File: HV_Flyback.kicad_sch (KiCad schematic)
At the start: 21 parts, among them J3 Conn_Coaxial, J4 Conn_01x01_Female, J5 Conn_01x01_Female, Q1 AON7296, U2 LT3750A, U4 AD5170BRMZ2.5

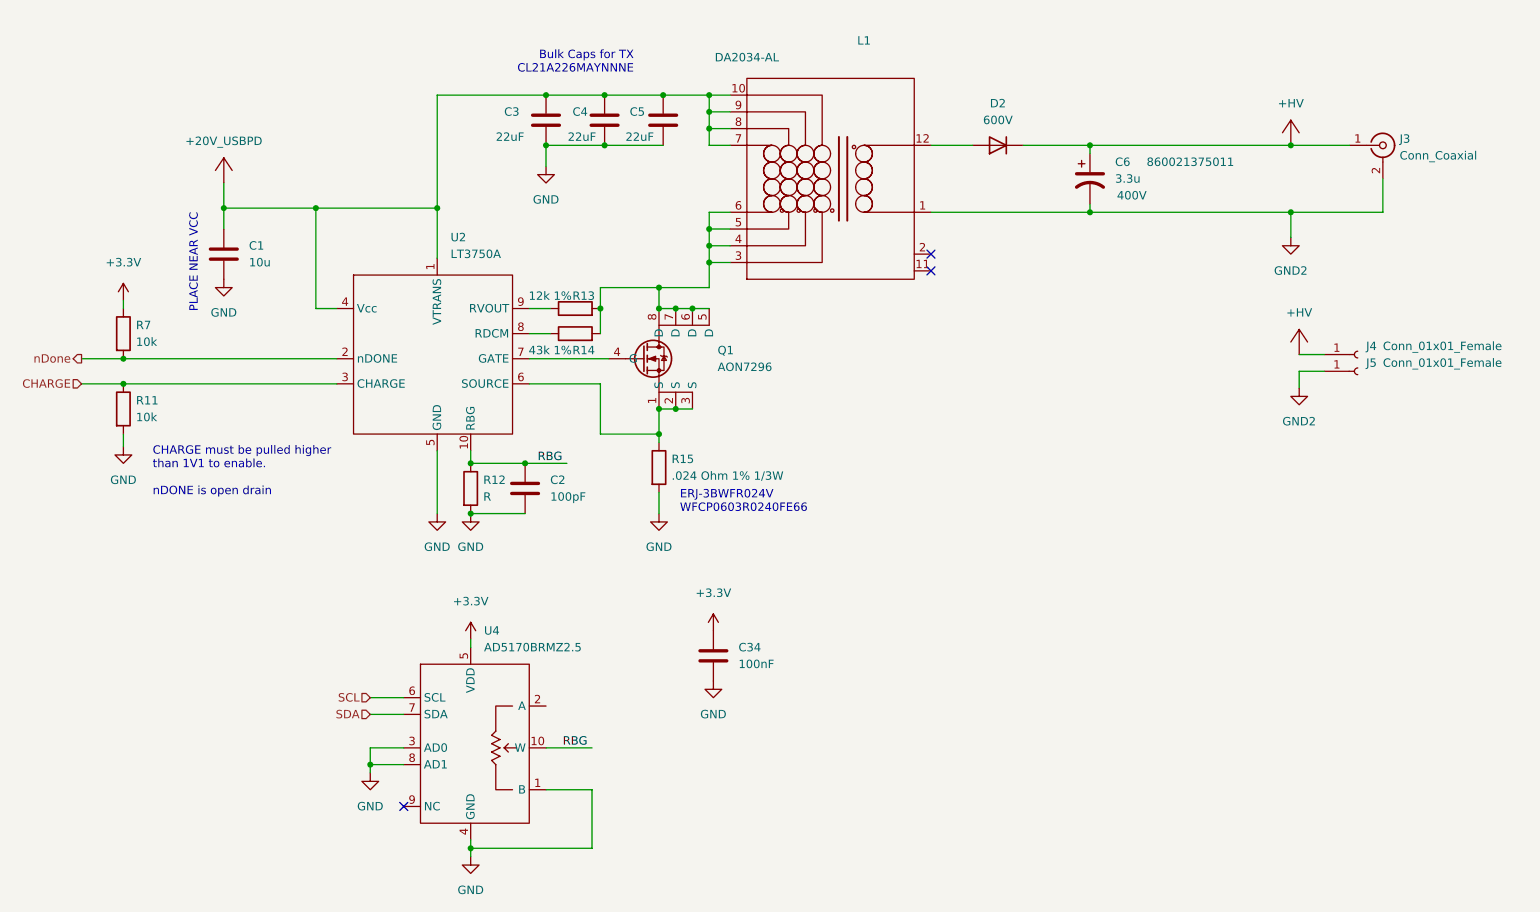
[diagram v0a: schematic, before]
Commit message: finished routing, sending to fab
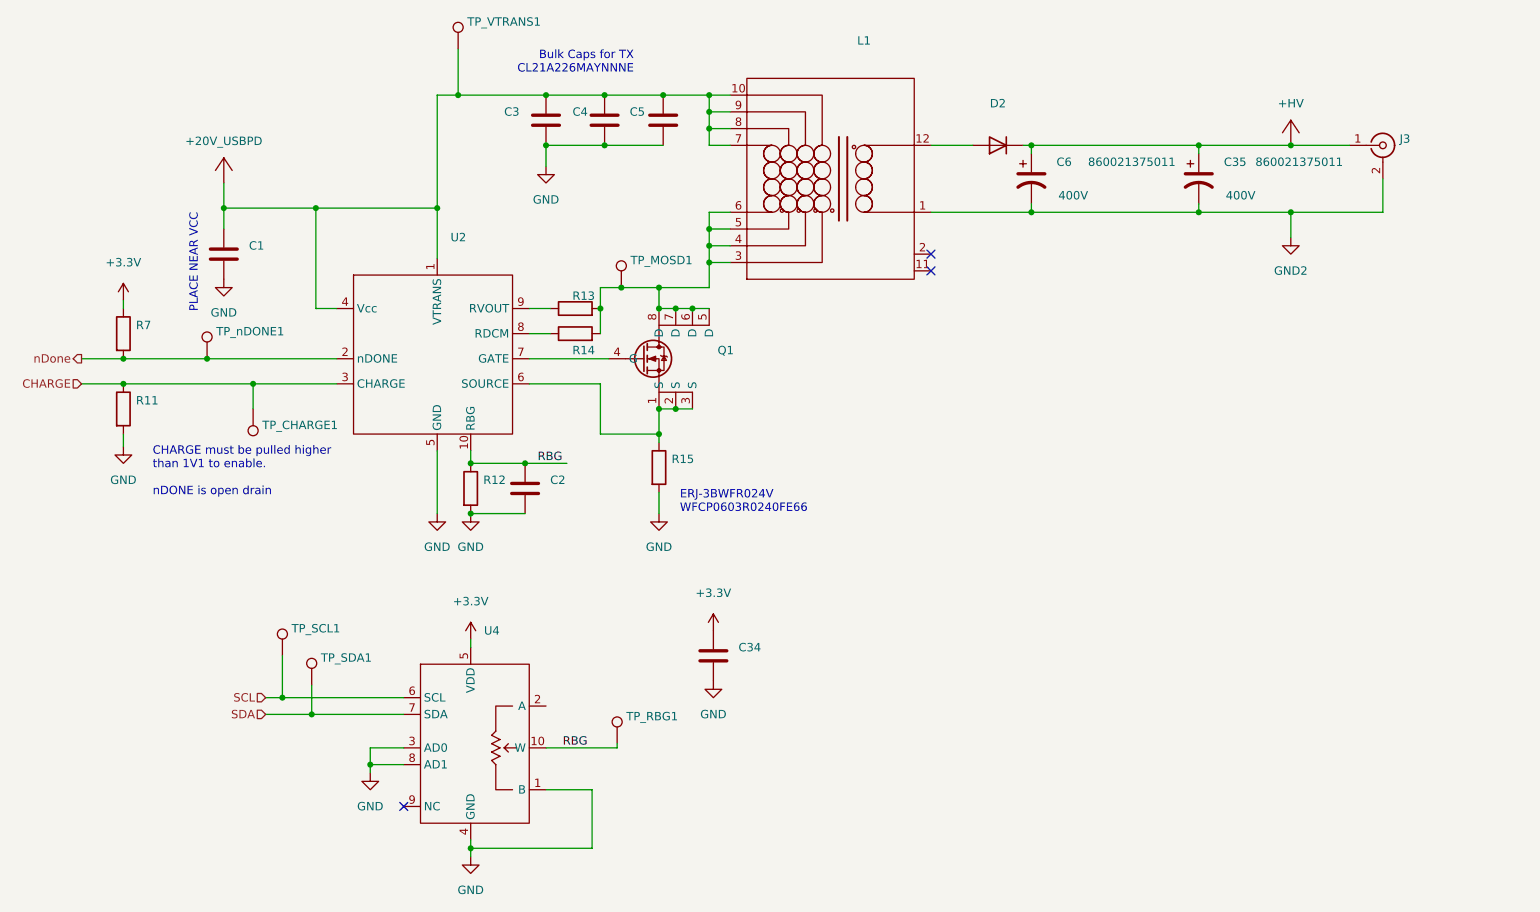
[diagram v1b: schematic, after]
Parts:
- removed J4: Conn_01x01_Female, PD_HV_footprints:CalTest_CT3151-2, symbol Connector:Conn_01x01_Female
- removed J5: Conn_01x01_Female, PD_HV_footprints:CalTest_CT3151-0, symbol Connector:Conn_01x01_Female
- added C35: (no value), symbol Device:C_Polarized_US
- added TP_CHARGE1, TP_MOSD1, TP_RBG1, TP_SCL1, TP_SDA1, TP_VTRANS1, TP_nDONE1: (no value), symbol Connector:TestPoint
- C1: value 10u -> (none); footprint Capacitor_SMD:C_0603_1608Metric -> (none)
- C2: value 100pF -> (none); footprint Capacitor_SMD:C_0603_1608Metric -> (none)
- C3, C4, C5: value 22uF -> (none); footprint Capacitor_SMD:C_0805_2012Metric -> (none)
- C34: value 100nF -> (none); footprint Capacitor_SMD:C_0603_1608Metric -> (none)
- C6: value 3.3u -> (none); footprint Capacitor_THT:CP_Radial_D10.0mm_P5.00mm -> (none)
- D2: value 600V -> (none); footprint Diode_SMD:D_SMA -> (none)
- J3: value Conn_Coaxial -> (none); footprint PD_HV_footprints:TE_5227161-2 -> (none)
- L1: value DA2034-AL -> (none); footprint PD_HV_footprints:DA2034-AL -> (none)
- Q1: value AON7296 -> (none); footprint PD_HV_footprints:DFN3X3A_8L_EPA1_P_AOS -> (none)
- R11, R7: value 10k -> (none); footprint Resistor_SMD:R_0603_1608Metric -> (none)
- R12: value R -> (none); footprint Resistor_SMD:R_0603_1608Metric -> (none)
- R13: value 12k 1% -> (none); footprint Resistor_SMD:R_0603_1608Metric -> (none)
- R14: value 43k 1% -> (none); footprint Resistor_SMD:R_0603_1608Metric -> (none)
- R15: value .024 Ohm 1% 1/3W -> (none); footprint Resistor_SMD:R_0603_1608Metric -> (none)
- U2: value LT3750A -> (none); footprint Package_SO:MSOP-10_3x3mm_P0.5mm -> (none)
- U4: value AD5170BRMZ2.5 -> (none); footprint Package_SO:MSOP-10_3x3mm_P0.5mm -> (none)
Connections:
- net +20V_USBPD: now also TP_VTRANS1.1
- net +HV: now also C35.1
- net CHARGE: now also TP_CHARGE1.1
- net GND2: now also C35.2
- net RBG: now also TP_RBG1.1
- net SCL: now also TP_SCL1.1
- net SDA: now also TP_SDA1.1
- net nDone: now also TP_nDONE1.1
- net at L1.3, L1.4, L1.5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: now also TP_MOSD1.1
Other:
- moved on the sheet: C6
